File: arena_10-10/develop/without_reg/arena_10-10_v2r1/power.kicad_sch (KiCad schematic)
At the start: 28 parts, among them J25 Barrel_Jack, J26 XT30 Female, SW1 SW_SPDT, U110 TLV6700, U111 TPS25982, U82 RB-XXYYD

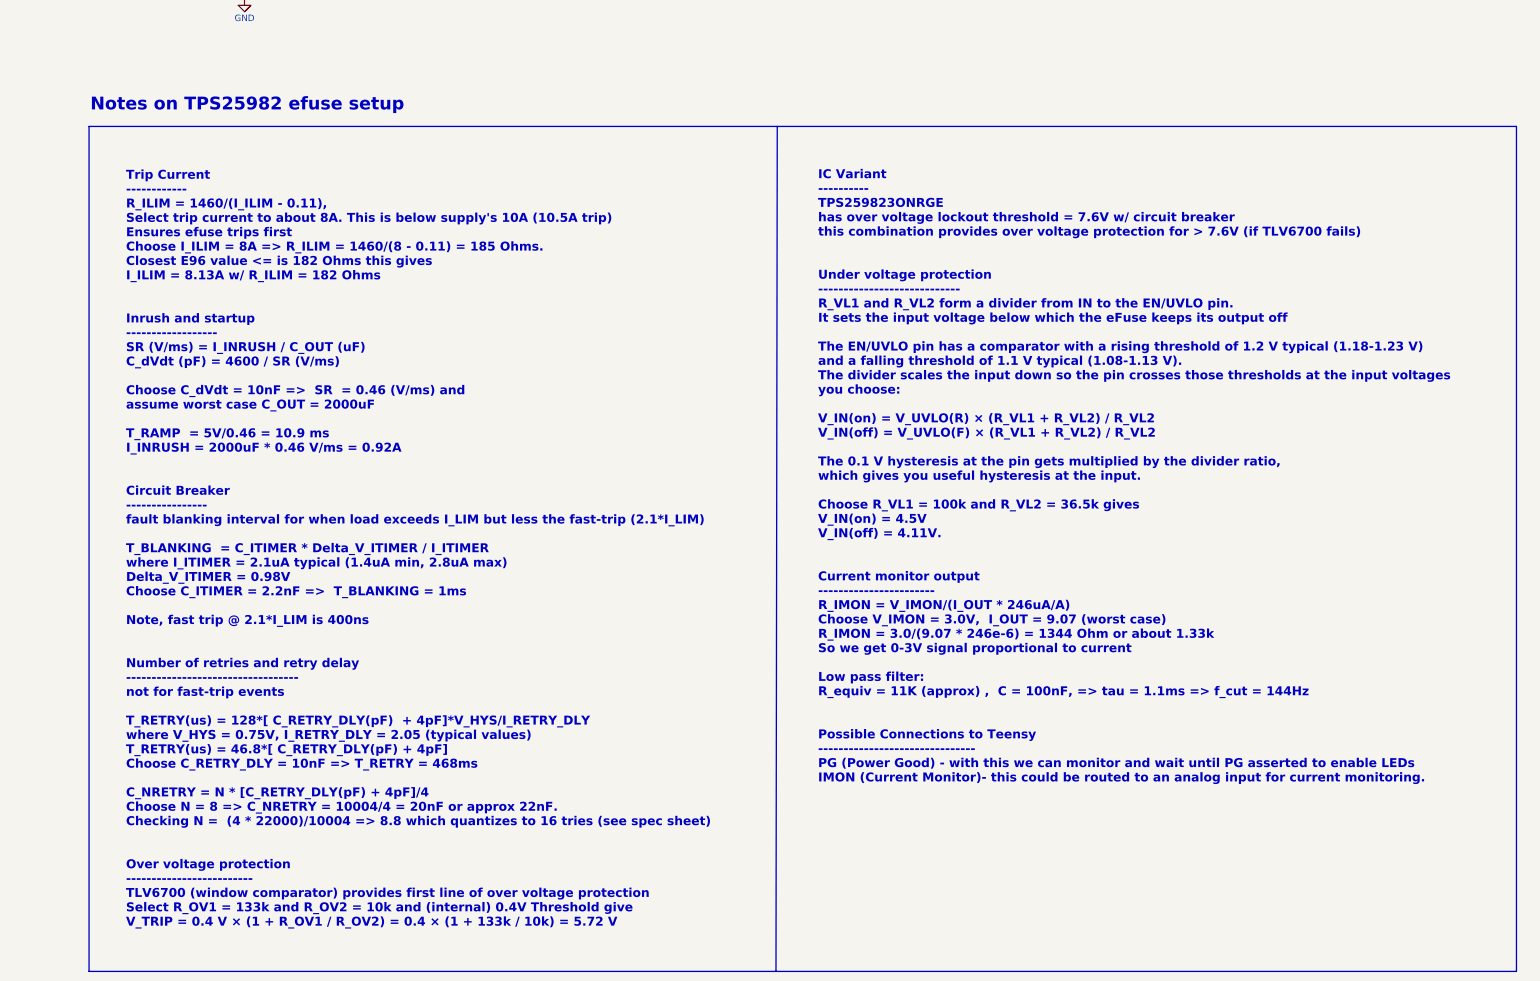
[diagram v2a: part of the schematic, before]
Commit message: Modified notes, moved XT30 connectors.
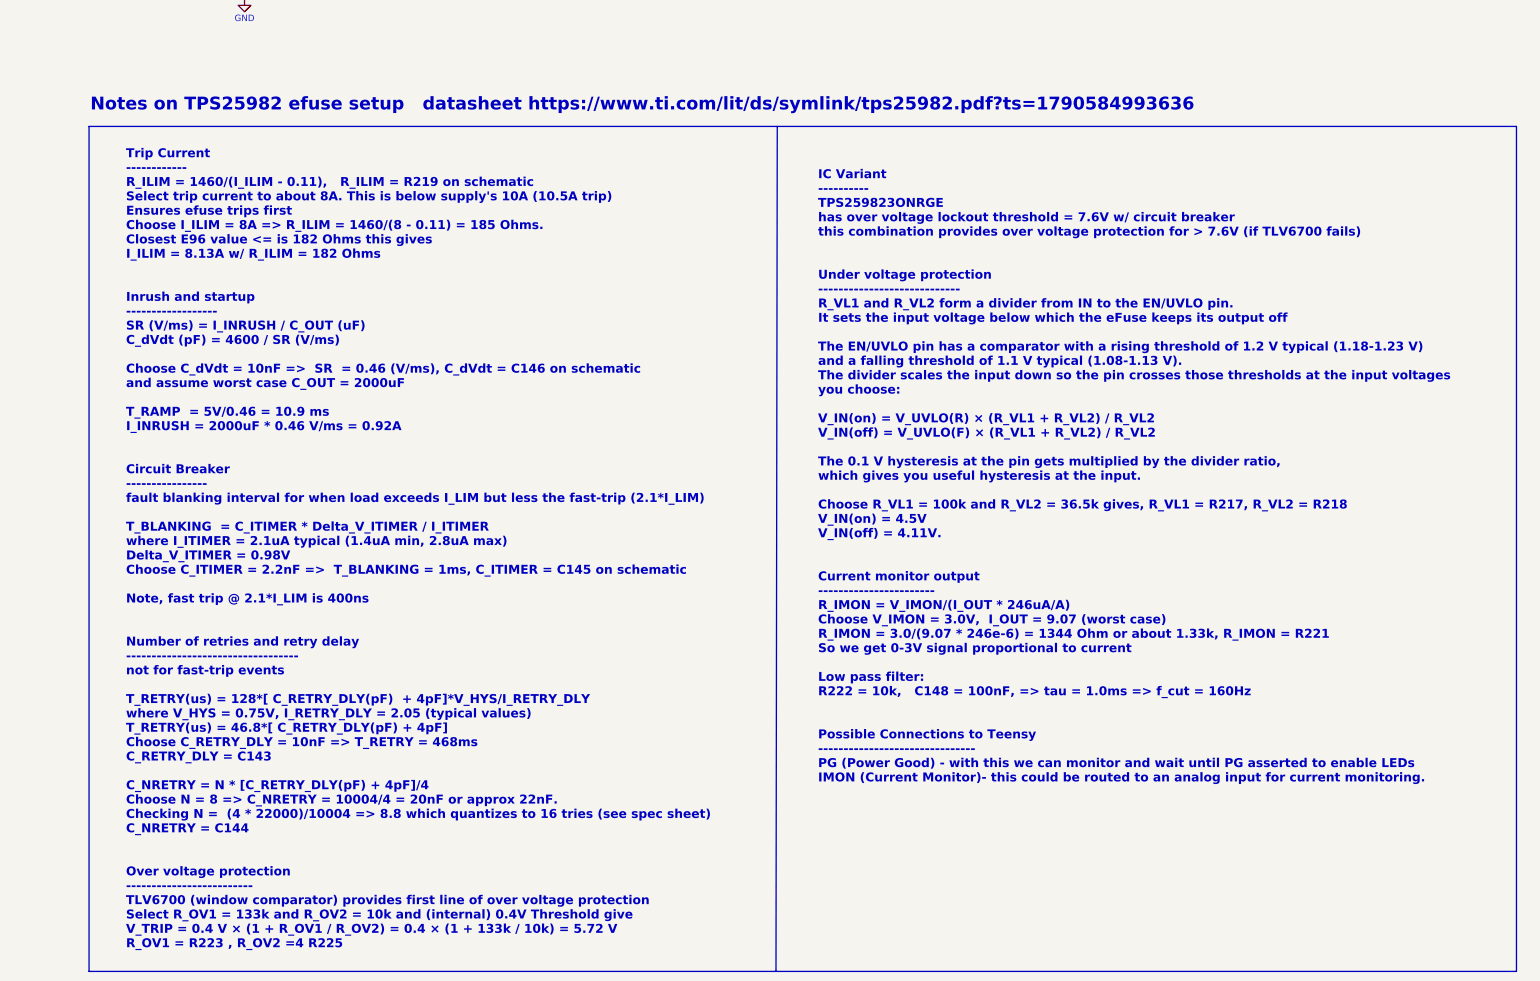
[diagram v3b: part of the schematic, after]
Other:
- note added: "Notes on TPS25982 efuse setup datasheet https://www.ti.com/lit/ds/symlink/tps25982.pdf?ts=1790584993636"
- note added: "Trip Current ------------ R_ILIM = 1460/(I_ILIM - 0.11), R_ILIM = R219 on schematic Select trip current to about 8A. This is below supply's 10A (10.5A trip) Ensures efuse trips first Choose I_ILIM = 8A => R_ILIM = 1460/(8 - 0.11) = 185 Ohms. Closest E96 value <= is 182 Ohms this gives I_ILIM = 8.13A w/ R_ILIM = 182 Ohms Inrush and startup ------------------ SR (V/ms) = I_INRUSH / C_OUT (uF) C_dVd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"
- note removed: "Notes on TPS25982 efuse setup"
- note removed: "Trip Current ------------ R_ILIM = 1460/(I_ILIM - 0.11), Select trip current to about 8A. This is below supply's 10A (10.5A trip) Ensures efuse trips first Choose I_ILIM = 8A => R_ILIM = 1460/(8 - 0.11) = 185 Ohms. Closest E96 value <= is 182 Ohms this gives I_ILIM = 8.13A w/ R_ILIM = 182 Ohms Inrush and startup ------------------ SR (V/ms) = I_INRUSH / C_OUT (uF) C_dVdt (pF) = 4600 / SR (V/ms) C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"
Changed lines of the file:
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@@
 		)
 	)
-	(text "Notes on TPS25982 efuse setup"
+	(text "Notes on TPS25982 efuse setup   datasheet https://www.ti.com/lit/ds/symlink/tps25982.pdf?ts=1790584993636"
 		(exclude_from_sim no)
 		(at 35.306 181.102 0)
@@
 		)
 	)
-	(text "IC Variant\n----------\nTPS259823ONRGE \nhas over voltage lockout threshold = 7.6V w/ circuit breaker\nthis combination provides over voltage protection for > 7.6V (if TLV6700 fails) \n\n\nUnder voltage protection\n----------------------------\nR_VL1 and R_VL2 form a divider from IN to the EN/UVLO pin. \nIt sets the input voltage below which the eFuse keeps its output off\n\nThe EN/UVLO pin has a comparator with a rising threshold of 1.2 V typical (1.18-1.23 V) \nand a falling threshold of 1.1 V typical (1.08-1.13 V). \nThe divider scales the input down so the pin crosses those thresholds at the input voltages \nyou choose:\n\nV_IN(on) = V_UVLO(R) × (R_VL1 + R_VL2) / R_VL2\nV_IN(off) = V_UVLO(F) × (R_VL1 + R_VL2) / R_VL2\n\nThe 0.1 V hysteresis at the pin gets multiplied by the divider ratio, \nwhich gives you useful hysteresis at the input.\n\nChoose R_VL1 = 100k and R_VL2 = 36.5k gives\nV_IN(on) = 4.5V\nV_IN(off) = 4.11V. \n\n\nCurrent monitor output\n-----------------------\nR_IMON = V_IMON/(I_OUT * 246uA/A)\nChoose V_IMON = 3.0V,  I_OUT = 9.07 (worst case)\nR_IMON = 3.0/(9.07 * 246e-6) = 1344 Ohm or about 1.33k \nSo we get 0-3V signal proportional to current\n\nLow pass filter:\nR_equiv = 11K (approx) ,  C = 100nF, => tau = 1.1ms => f_cut = 144Hz\n\n\nPossible Connections to Teensy\n-------------------------------\nPG (Power Good) - with this we can monitor and wait until PG asserted to enable LEDs\nIMON (Current Monitor)- this could be routed to an analog input for current monitoring. \n"
+	(text "IC Variant\n----------\nTPS259823ONRGE \nhas over voltage lockout threshold = 7.6V w/ circuit breaker\nthis combination provides over voltage protection for > 7.6V (if TLV6700 fails) \n\n\nUnder voltage protection\n----------------------------\nR_VL1 and R_VL2 form a divider from IN to the EN/UVLO pin. \nIt sets the input voltage below which the eFuse keeps its output off\n\nThe EN/UVLO pin has a comparator with a rising threshold of 1.2 V typical (1.18-1.23 V) \nand a falling threshold of 1.1 V typical (1.08-1.13 V). \nThe divider scales the input down so the pin crosses those thresholds at the input voltages \nyou choose:\n\nV_IN(on) = V_UVLO(R) × (R_VL1 + R_VL2) / R_VL2\nV_IN(off) = V_UVLO(F) × (R_VL1 + R_VL2) / R_VL2\n\nThe 0.1 V hysteresis at the pin gets multiplied by the divider ratio, \nwhich gives you useful hysteresis at the input.\n\nChoose R_VL1 = 100k and R_VL2 = 36.5k gives, R_VL1 = R217, R_VL2 = R218\nV_IN(on) = 4.5V\nV_IN(off) = 4.11V. \n\n\nCurrent monitor output\n-----------------------\nR_IMON = V_IMON/(I_OUT * 246uA/A)\nChoose V_IMON = 3.0V,  I_OUT = 9.07 (worst case)\nR_IMON = 3.0/(9.07 * 246e-6) = 1344 Ohm or about 1.33k, R_IMON = R221\nSo we get 0-3V signal proportional to current\n\nLow pass filter:\nR222 = 10k,   C148 = 100nF, => tau = 1.0ms => f_cut = 160Hz\n\n\nPossible Connections to Teensy\n-------------------------------\nPG (Power Good) - with this we can monitor and wait until PG asserted to enable LEDs\nIMON (Current Monitor)- this could be routed to an analog input for current monitoring. \n"
 		(exclude_from_sim no)
 		(at 180.34 255.27 0)
@@
 		)
 	)
-	(text "\nTrip Current\n------------\nR_ILIM = 1460/(I_ILIM - 0.11),   \nSelect trip current to about 8A. This is below supply's 10A (10.5A trip)\nEnsures efuse trips first\nChoose I_ILIM = 8A => R_ILIM = 1460/(8 - 0.11) = 185 Ohms. \nClosest E96 value <= is 182 Ohms this gives\nI_ILIM = 8.13A w/ R_ILIM = 182 Ohms\n\n\nInrush and startup\n------------------\nSR (V/ms) = I_INRUSH / C_OUT (uF)\nC_dVdt (pF) = 4600 / SR (V/ms)\n\nChoose C_dVdt = 10nF =>  SR  = 0.46 (V/ms) and \nassume worst case C_OUT = 2000uF \n\nT_RAMP  = 5V/0.46 = 10.9 ms\nI_INRUSH = 2000uF * 0.46 V/ms = 0.92A\n\n\nCircuit Breaker\n----------------\nfault blanking interval for when load exceeds I_LIM but less the fast-trip (2.1*I_LIM)\n\nT_BLANKING  = C_ITIMER * Delta_V_ITIMER / I_ITIMER\nwhere I_ITIMER = 2.1uA typical (1.4uA min, 2.8uA max) \nDelta_V_ITIMER = 0.98V\nChoose C_ITIMER = 2.2nF =>  T_BLANKING = 1ms\n\nNote, fast trip @ 2.1*I_LIM is 400ns\n\n\nNumber of retries and retry delay\n----------------------------------\nnot for fast-trip events\n\nT_RETRY(us) = 128*[ C_RETRY_DLY(pF)  + 4pF]*V_HYS/I_RETRY_DLY\nwhere V_HYS = 0.75V, I_RETRY_DLY = 2.05 (typical values)\nT_RETRY(us) = 46.8*[ C_RETRY_DLY(pF) + 4pF]\nChoose C_RETRY_DLY = 10nF => T_RETRY = 468ms\n\nC_NRETRY = N * [C_RETRY_DLY(pF) + 4pF]/4 \nChoose N = 8 => C_NRETRY = 10004/4 = 20nF or approx 22nF. \nChecking N =  (4 * 22000)/10004 => 8.8 which quantizes to 16 tries (see spec sheet)  \n\n\nOver voltage protection\n-------------------------\nTLV6700 (window comparator) provides first line of over voltage protection  \nSelect R_OV1 = 133k and R_OV2 = 10k and (internal) 0.4V Threshold give\nV_TRIP = 0.4 V × (1 + R_OV1 / R_OV2) = 0.4 × (1 + 133k / 10k) = 5.72 V\n\n\n\n\n\n\n"
+	(text "\nTrip Current\n------------\nR_ILIM = 1460/(I_ILIM - 0.11),   R_ILIM = R219 on schematic\nSelect trip current to about 8A. This is below supply's 10A (10.5A trip)\nEnsures efuse trips first\nChoose I_ILIM = 8A => R_ILIM = 1460/(8 - 0.11) = 185 Ohms. \nClosest E96 value <= is 182 Ohms this gives\nI_ILIM = 8.13A w/ R_ILIM = 182 Ohms\n\n\nInrush and startup\n------------------\nSR (V/ms) = I_INRUSH / C_OUT (uF)\nC_dVdt (pF) = 4600 / SR (V/ms)\n\nChoose C_dVdt = 10nF =>  SR  = 0.46 (V/ms), C_dVdt = C146 on schematic\nand assume worst case C_OUT = 2000uF \n\nT_RAMP  = 5V/0.46 = 10.9 ms\nI_INRUSH = 2000uF * 0.46 V/ms = 0.92A\n\n\nCircuit Breaker\n----------------\nfault blanking interval for when load exceeds I_LIM but less the fast-trip (2.1*I_LIM)\n\nT_BLANKING  = C_ITIMER * Delta_V_ITIMER / I_ITIMER\nwhere I_ITIMER = 2.1uA typical (1.4uA min, 2.8uA max) \nDelta_V_ITIMER = 0.98V\nChoose C_ITIMER = 2.2nF =>  T_BLANKING = 1ms, C_ITIMER = C145 on schematic\n\nNote, fast trip @ 2.1*I_LIM is 400ns\n\n\nNumber of retries and retry delay\n----------------------------------\nnot for fast-trip events\n\nT_RETRY(us) = 128*[ C_RETRY_DLY(pF)  + 4pF]*V_HYS/I_RETRY_DLY\nwhere V_HYS = 0.75V, I_RETRY_DLY = 2.05 (typical values)\nT_RETRY(us) = 46.8*[ C_RETRY_DLY(pF) + 4pF]\nChoose C_RETRY_DLY = 10nF => T_RETRY = 468ms\nC_RETRY_DLY = C143\n\nC_NRETRY = N * [C_RETRY_DLY(pF) + 4pF]/4 \nChoose N = 8 => C_NRETRY = 10004/4 = 20nF or approx 22nF. \nChecking N =  (4 * 22000)/10004 => 8.8 which quantizes to 16 tries (see spec sheet)  \nC_NRETRY = C144\n\n\nOver voltage protection\n-------------------------\nTLV6700 (window comparator) provides first line of over voltage protection  \nSelect R_OV1 = 133k and R_OV2 = 10k and (internal) 0.4V Threshold give\nV_TRIP = 0.4 V × (1 + R_OV1 / R_OV2) = 0.4 × (1 + 133k / 10k) = 5.72 V\nR_OV1 = R223 , R_OV2 =4 R225\n\n\n\n\n\n\n"
 		(exclude_from_sim no)
 		(at 42.418 276.86 0)

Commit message: Made modifications to efuse circuit and added some notes.
Modified efuse so that switch is now is EN/UVLO leg. Added 1k
resistors for extra wetting current - so we can use any old switch.
Upped capacitors size to help with switch debounce. Added 1k resistor
between TVL6700 and EN/UVLO. This is to deal with current when OUTB
discharges the larger EN capacitor.
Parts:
- added R226, R227: 1k, Resistor_SMD:R_0402_1005Metric, symbol Device:R
- C142: value 0.1uF, >=25V -> 0.1uF >=25V
- C150: value 10nF -> 100nF
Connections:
- net GND: now also R226.2
- net IN: now also SW1.1 (A); no longer R217.1
- net at C150.1, R217.2, R218.1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: now also R227.2; no longer SW1.2 (B), U110.6 (OUTB)
- new net: R217.1, R226.1, SW1.2 (B)
- new net: R227.1, U110.6 (OUTB)
- no-connect marks 2 -> 1
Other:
- moved on the sheet: C142, C143, C144, C145, C146, C147, C148, C149, C150, C151, D5, D6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

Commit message: Added clamp to IMON.  Connected PG and IMON to teensy.
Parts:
- added D8: BAS40-04, Package_TO_SOT_SMD:SOT-23, symbol Diode:BAS40-04
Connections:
- net +3.3V: now also D8.2
- net GND: now also D8.1
- net IMON: now also D8.3
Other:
- note added: "Power Monitoring Signals"
- moved on the sheet: J26, U82

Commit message: Added analog island to 10-10 arena with efuse.
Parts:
- added J32: XT30 Female, Connector_JST:JST_PH_B2B-PH-K_1x02_P2.00mm_Vertical, symbol Connector_Generic:Conn_01x02
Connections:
- net +5V: now also J32.1 (Pin_1)
- net GND: now also J32.2 (Pin_2)
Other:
- note added: "JST PH 2-pin aux power"
